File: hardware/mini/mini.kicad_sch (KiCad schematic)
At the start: 0 parts

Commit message: mini
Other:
- added sheet mcu (mcu.kicad_sch)
- added sheet measurement (measurement.kicad_sch)
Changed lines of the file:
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@@
 	(paper "A4")
+	(sheet
+		(at 167.005 82.55)
+		(size 35.56 33.655)
+		(fields_autoplaced yes)
+		(stroke
+			(width 0.1524)
+			(type solid)
+		)
+		(fill
+			(color 0 0 0 0.0000)
+		)
+		(property "Sheetname" "mcu"
+			(at 167.005 81.8384 0)
+			(effects
+				(font
+					(size 1.27 1.27)
+				)
+				(justify left bottom)
+			)
+		)
+		(property "Sheetfile" "mcu.kicad_sch"
+			(at 167.005 116.7896 0)
+			(effects
+				(font
+					(size 1.27 1.27)
+				)
+				(justify left top)
+			)
+		)
+		(instances
+			(project "mini"
+				(path "/5aaaac9a-5acd-4aef-ad51-a6d04aa88705"
+					(page "4")
+				)
+			)
+		)
+	)
 	(sheet
 		(at 87.63 83.82)
@@
 				)
 			)
+		)
+	)
+	(sheet
+		(at 223.52 89.535)
+		(size 22.86 26.035)
+		(fields_autoplaced yes)
+		(stroke
+			(width 0.1524)
+			(type solid)
+		)
+		(fill
+			(color 0 0 0 0.0000)
+		)
+		(property "Sheetname" "measurement"
+			(at 223.52 88.8234 0)
+			(effects
+				(font
+					(size 1.27 1.27)
+				)
+				(justify left bottom)
+			)
+		)
+		(property "Sheetfile" "measurement.kicad_sch"
+			(at 223.52 116.1546 0)
+			(effects
+				(font
+					(size 1.27 1.27)
+				)
+				(justify left top)
+			)
+		)
+		(instances
+			(project "mini"
+				(path "/5aaaac9a-5acd-4aef-ad51-a6d04aa88705"
+					(page "5")
+				)
+			)

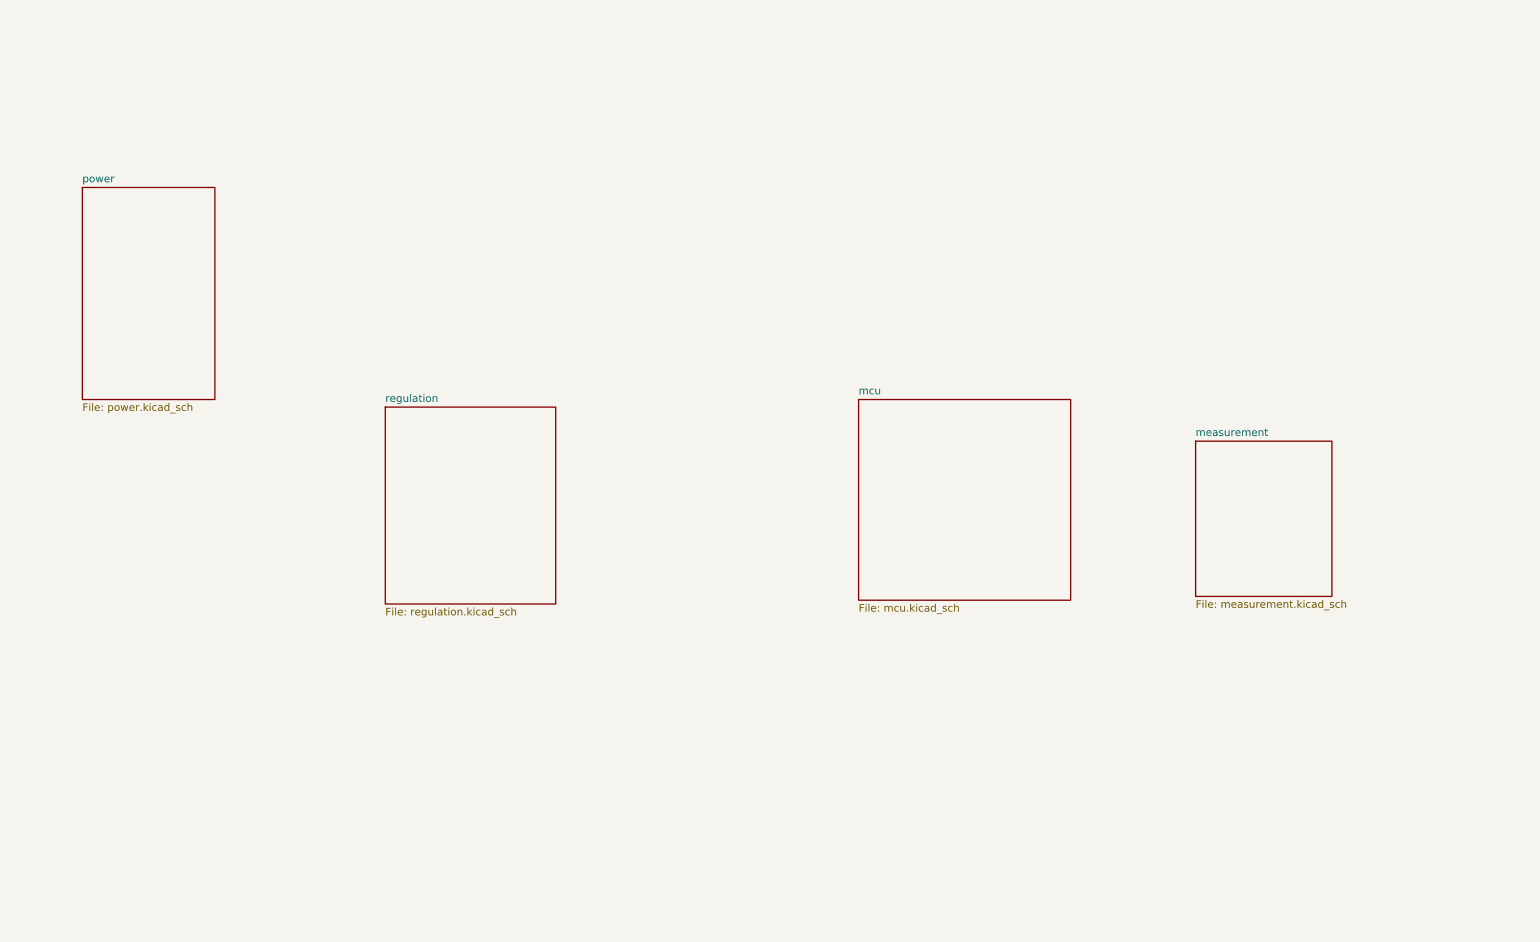
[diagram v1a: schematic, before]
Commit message: add interface & RP2040
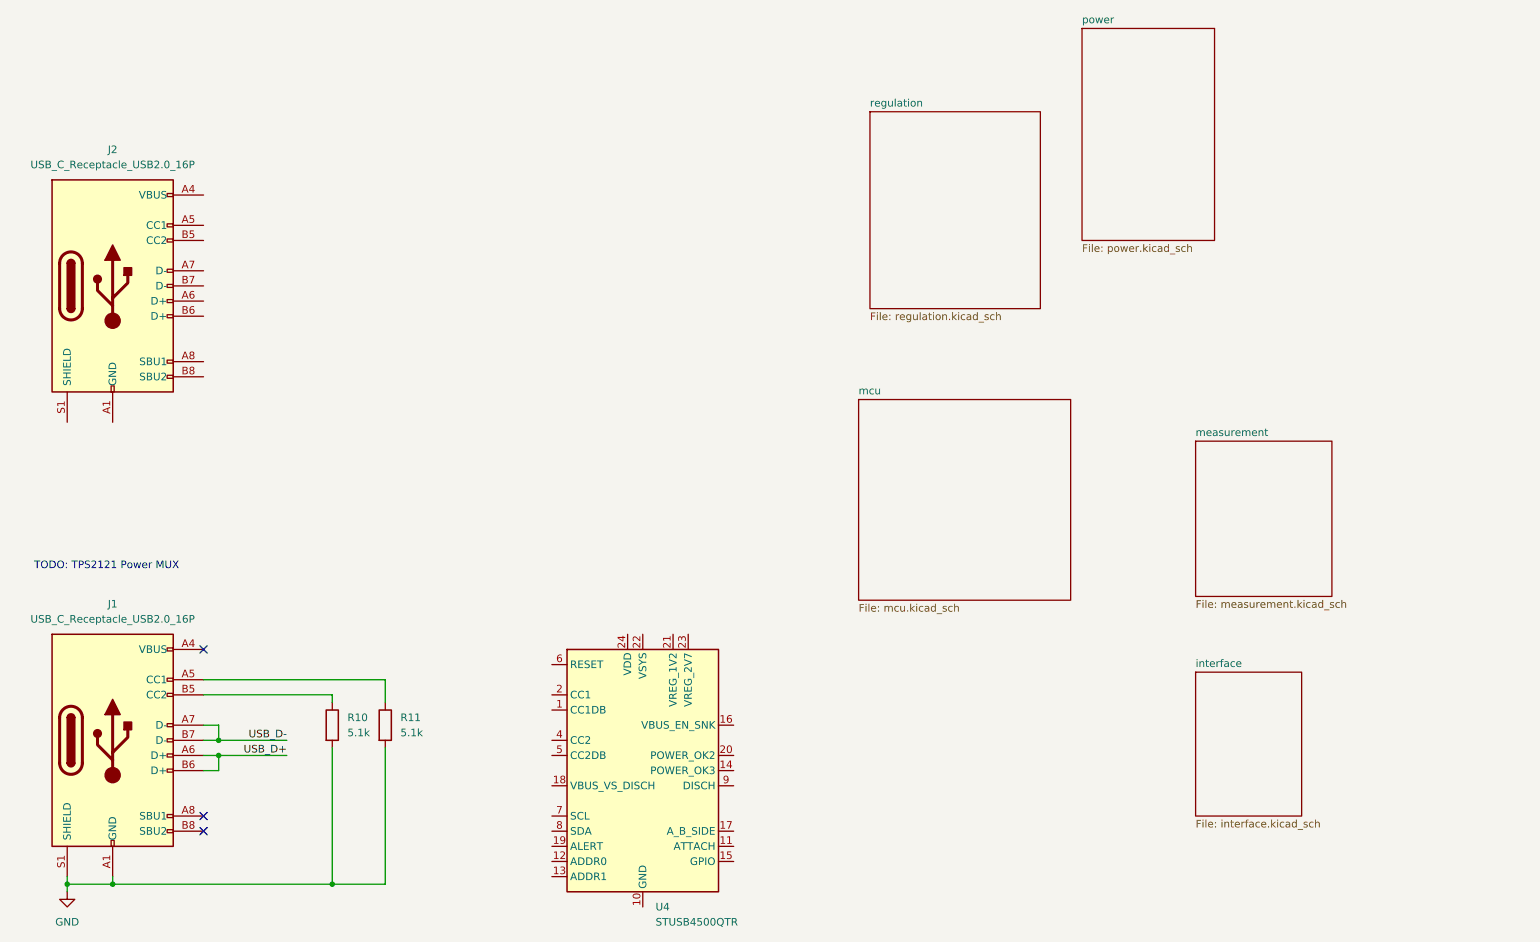
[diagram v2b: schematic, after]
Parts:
- added J1, J2: USB_C_Receptacle_USB2.0_16P, symbol Connector:USB_C_Receptacle_USB2.0_16P
- added R10, R11: 5.1k, symbol Device:R
- added U4: STUSB4500QTR, Package_DFN_QFN:QFN-24-1EP_4x4mm_P0.5mm_EP2.7x2.7mm, symbol Interface_USB:STUSB4500QTR
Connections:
- new net: J1.A4 (VBUS), J1.A9 (VBUS), J1.B4 (VBUS), J1.B9 (VBUS)
- new net: J1.A5 (CC1), R11.1
- new net: J1.B5 (CC2), R10.1
- new net: J2.A1 (GND), J2.A12 (GND), J2.B1 (GND), J2.B12 (GND)
- new net: J2.A4 (VBUS), J2.A9 (VBUS), J2.B4 (VBUS), J2.B9 (VBUS)
- new net: U4.10 (GND), U4.25 (GND)
- new net GND: J1.A1 (GND), J1.A12 (GND), J1.B1 (GND), J1.B12 (GND), J1.S1 (SHIELD), R10.2, R11.2
- new net USB_D+: J1.A6 (D+), J1.B6 (D+)
- new net USB_D-: J1.A7 (D-), J1.B7 (D-)
- no-connect marks 0 -> 3
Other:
- added sheet interface (interface.kicad_sch)
- note added: "TODO: TPS2121 Power MUX"

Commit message: finalize parts in schematic
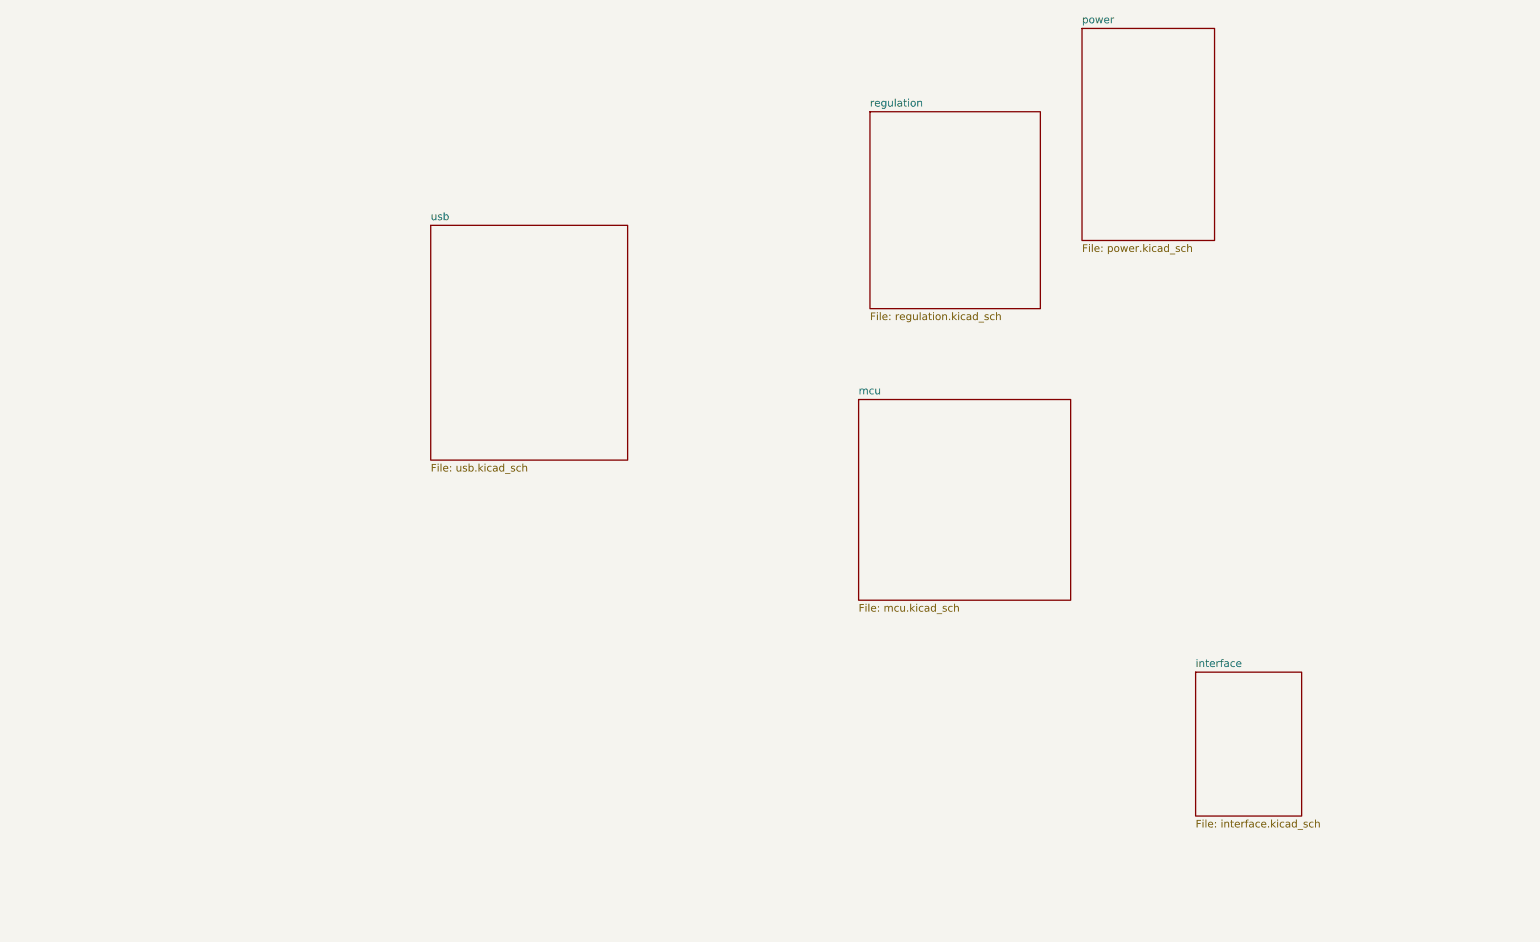
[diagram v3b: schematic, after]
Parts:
- removed J1, J2: USB_C_Receptacle_USB2.0_16P, symbol Connector:USB_C_Receptacle_USB2.0_16P
- removed R10, R11: 5.1k, symbol Device:R
- removed U4: STUSB4500QTR, Package_DFN_QFN:QFN-24-1EP_4x4mm_P0.5mm_EP2.7x2.7mm, symbol Interface_USB:STUSB4500QTR
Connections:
- no-connect marks 3 -> 0
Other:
- removed sheet measurement
- added sheet usb (usb.kicad_sch)
- note removed: "TODO: TPS2121 Power MUX"

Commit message: route most
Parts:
- added J3, J4: Conn_02x05_Odd_Even, symbol Connector_Generic:Conn_02x05_Odd_Even
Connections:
- new net GNDPWR: J3.10 (Pin_10), J3.2 (Pin_2), J3.4 (Pin_4), J3.6 (Pin_6), J3.8 (Pin_8), J4.10 (Pin_10), J4.2 (Pin_2), J4.4 (Pin_4), J4.6 (Pin_6), J4.8 (Pin_8)
- new net channel_A/VOUT_SENSE: J3.1 (Pin_1), J3.3 (Pin_3), J3.5 (Pin_5), J3.7 (Pin_7), J3.9 (Pin_9)
- new net channel_B/VOUT_SENSE: J4.1 (Pin_1), J4.3 (Pin_3), J4.5 (Pin_5), J4.7 (Pin_7), J4.9 (Pin_9)
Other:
- removed sheet power
- added sheet channel_A (power.kicad_sch)
- added sheet channel_B (power.kicad_sch)
- sheet interface ports: added BACKLIGHT, COL_0, COL_1, CS, LED_DIN, ROW_0, ROW_1, ROW_2, ROW_3, ROW_4, RS, RST, SCL, SDA; removed none
- sheet mcu ports: added COL_0, COL_1, DISP_BACKLIGHT, DISP_RS, DISP_RST, EN_A, EN_B, I2C0_SCL, I2C0_SDA, I2C1_SCL, I2C1_SDA, ROW_0, ROW_1, ROW_2, ROW_3, ROW_4, SENS_INT_A, SENS_INT_B, SPI0_CS, SPI0_RX, SPI0_SCK, SPI0_TX, SWCLK, SWD, TEMP_A, TEMP_B, USB_D+, USB_D-, USB_INT; removed none
- sheet usb ports: added ALERT, RESET, SCL, SDA, USB_D+, USB_D-; removed none
- note added: "ADDR: 0x40"
- note added: "ADDR: 0x41"
- note added: "ADDR: 0x74"
- note added: "ADDR: 0x75"

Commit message: ERC run
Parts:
- added FID1, FID2, FID3, FID4: Fiducial, symbol Mechanical:Fiducial
- added J1: Conn_01x03, symbol Connector_Generic:Conn_01x03
- renumbered J3 to J2, J4 to J3
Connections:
- net GND: now also J1.2 (Pin_2)
- net mcu/SWCLK: now also J1.1 (Pin_1)
- net mcu/SWD: now also J1.3 (Pin_3)
- no-connect marks 0 -> 1
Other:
- sheet channel_A ports: added CONVERTER_VCC; removed none
- sheet channel_B ports: added CONVERTER_VCC; removed none
- sheet mcu ports: added LED_DATA, USB_RST; removed SPI0_RX

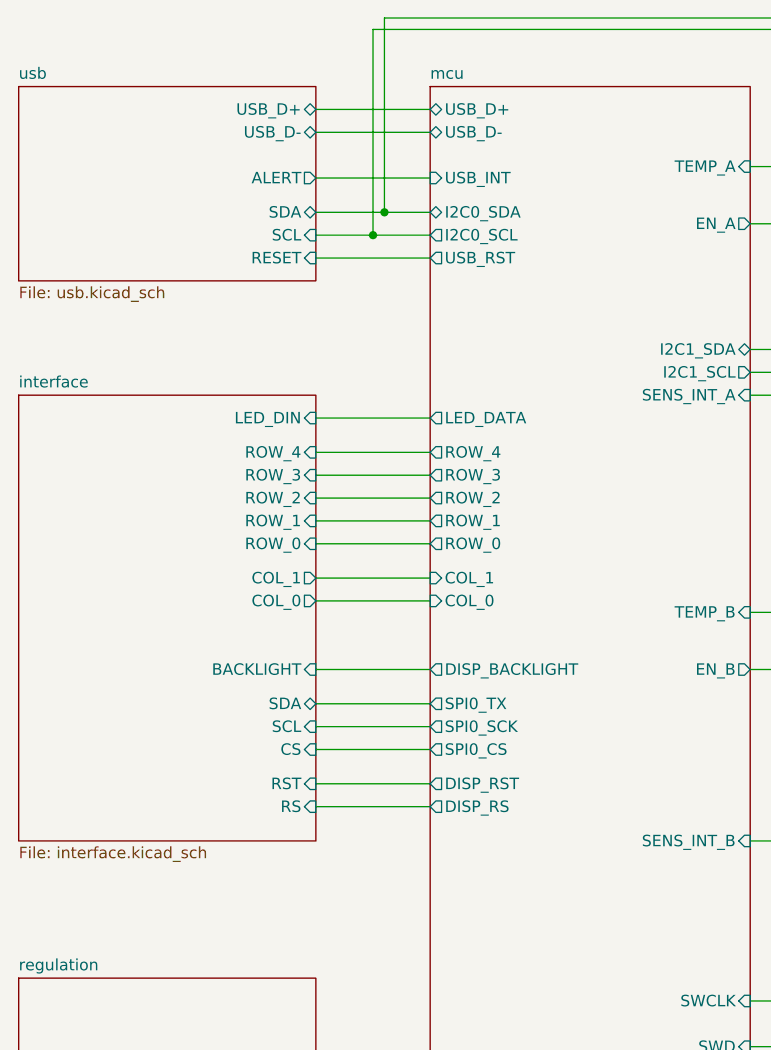
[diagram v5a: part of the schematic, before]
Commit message: assign footprints & LCSC id
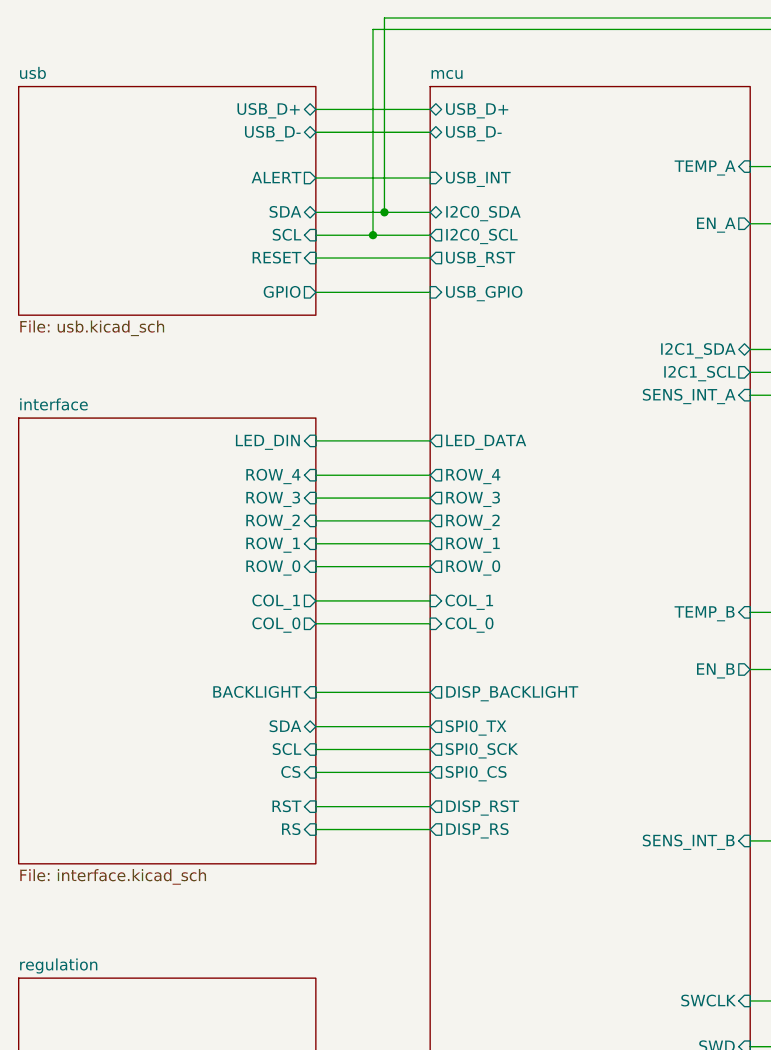
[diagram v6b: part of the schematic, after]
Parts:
- J2, J3: footprint (none) -> Connector_PinHeader_2.54mm:PinHeader_2x05_P2.54mm_Vertical_SMD; LCSC (none) -> C124391
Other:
- sheet mcu ports: added USB_GPIO; removed none
- sheet usb ports: added GPIO; removed none

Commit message: import to PCB
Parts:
- FID1, FID2, FID3, FID4: footprint (none) -> Fiducial:Fiducial_1mm_Mask2mm
- J1: footprint (none) -> Jumper:SolderJumper-3_P1.3mm_Open_RoundedPad1.0x1.5mm
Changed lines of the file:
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@@
 			)
 		)
-		(property "Footprint" ""
+		(property "Footprint" "Fiducial:Fiducial_1mm_Mask2mm"
 			(at 266.7 152.4 0)
 			(effects
@@
 			)
 		)
-		(property "Footprint" ""
+		(property "Footprint" "Fiducial:Fiducial_1mm_Mask2mm"
 			(at 254 152.4 0)
 			(effects
@@
 			)
 		)
-		(property "Footprint" ""
+		(property "Footprint" "Fiducial:Fiducial_1mm_Mask2mm"
 			(at 254 157.48 0)
 			(effects
@@
 			)
 		)
-		(property "Footprint" ""
+		(property "Footprint" "Fiducial:Fiducial_1mm_Mask2mm"
 			(at 266.7 157.48 0)
 			(effects
@@
 			)
 		)
-		(property "Footprint" ""
+		(property "Footprint" "Jumper:SolderJumper-3_P1.3mm_Open_RoundedPad1.0x1.5mm"
 			(at 152.4 151.13 0)
 			(effects

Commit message: place ui elements
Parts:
- added H1, H2, H3, H4: M3, MountingHole:MountingHole_3.2mm_M3_DIN965_Pad_TopBottom, symbol Mechanical:MountingHole_Pad
- added N1: LCD, protovolt_mini_fp:HS20HS072RX, symbol Mechanical:Housing
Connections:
- net GNDPWR: now also H1.1, H2.1, H3.1, H4.1
